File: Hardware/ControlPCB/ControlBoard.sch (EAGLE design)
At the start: 14 parts, among them IC1 TPS774

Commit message: Some PCB changes
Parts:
- added R7: 36k, resistor:R-EU_M2012
- added S2: DTSM-6, switch-tact:DTSM-6
- R4, R5: value (none) -> 0
- S1: device SparkFun-Electromechanical:SWITCH-MOMENTARY-2SMD-2 -> switch-tact:DTSM-6
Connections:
- net !RST: now also S2.1, S2.2
- net GND: now also R7.2, S1.2, S2.3, S2.4; no longer X2-4.1
- net GPIO0: now also S1.3, S1.4; no longer S1.2
- net OE: now also R7.1
- net VCC: now also X2-4.1
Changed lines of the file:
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@@
 <part name="R2" library="resistor" deviceset="R-EU_" device="R1206" value="4.7K"/>
 <part name="R3" library="resistor" deviceset="R-EU_" device="R1206" value="4.7K"/>
-<part name="S1" library="SparkFun-Electromechanical" deviceset="SWITCH-MOMENTARY-2" device="SMD-2" value="FlashSW"/>
+<part name="S1" library="switch-tact" deviceset="DTSM-6" device="" value="FlashSW"/>
 <part name="U1" library="esp8266modules" deviceset="ESP12E" device="SMD"/>
 <part name="IC1" library="texas" deviceset="TPS774*" device=""/>
@@
 <part name="X1" library="con-amp" deviceset="SMDTOP-20" device=""/>
 <part name="X2" library="con-amp" deviceset="SMDTOP-4" device=""/>
-<part name="R4" library="resistor" deviceset="R-EU_" device="R5025W"/>
-<part name="R5" library="resistor" deviceset="R-EU_" device="R5025W"/>
+<part name="R4" library="resistor" deviceset="R-EU_" device="R5025W" value="0"/>
+<part name="R5" library="resistor" deviceset="R-EU_" device="R5025W" value="0"/>
 <part name="R6" library="SparkFun-Passives" deviceset="SOLDERJUMPER" device="TRACE" value=""/>
 <part name="SJ1" library="SparkFun-Passives" deviceset="SOLDERJUMPER" device="TRACE" value=""/>
+<part name="R7" library="resistor" deviceset="R-EU_" device="M2012" value="36k"/>
+<part name="S2" library="switch-tact" deviceset="DTSM-6" device=""/>
 </parts>
 <sheets>
@@
 <instance part="R2" gate="G$1" x="88.9" y="119.38" rot="R180"/>
 <instance part="R3" gate="G$1" x="88.9" y="127" rot="R180"/>
-<instance part="S1" gate="G$1" x="88.9" y="142.24" rot="MR0"/>
+<instance part="S1" gate="G$1" x="88.9" y="142.24" rot="MR270"/>
 <instance part="U1" gate="G$1" x="101.6" y="104.14"/>
 <instance part="IC1" gate="G$1" x="160.02" y="137.16"/>
@@
 <instance part="R6" gate="1" x="154.94" y="99.06"/>
 <instance part="SJ1" gate="1" x="154.94" y="93.98"/>
+<instance part="R7" gate="G$1" x="154.94" y="116.84"/>
+<instance part="S2" gate="G$1" x="88.9" y="154.94" rot="R270"/>
 </instances>
 <busses>
@@
 <label x="96.52" y="142.24" size="1.778" layer="95"/>
 <pinref part="S1" gate="G$1" pin="1"/>
+<pinref part="S1" gate="G$1" pin="2"/>
+<wire x1="93.98" y1="139.7" x2="93.98" y2="142.24" width="0.1524" layer="91"/>
 </segment>
 <segment>
@@
 </segment>
 <segment>
-<pinref part="X2" gate="-4" pin="1"/>
-<wire x1="127" y1="134.62" x2="121.92" y2="134.62" width="0.1524" layer="91"/>
+<pinref part="R7" gate="G$1" pin="2"/>
+<wire x1="160.02" y1="116.84" x2="165.1" y2="116.84" width="0.1524" layer="91"/>
+<label x="165.1" y="116.84" size="1.778" layer="95"/>
+</segment>
+<segment>
+<pinref part="S2" gate="G$1" pin="3"/>
+<wire x1="93.98" y1="154.94" x2="96.52" y2="154.94" width="0.1524" layer="91"/>
+<pinref part="S2" gate="G$1" pin="4"/>
+<wire x1="93.98" y1="152.4" x2="93.98" y2="154.94" width="0.1524" layer="91"/>
+<label x="96.52" y="154.94" size="1.778" layer="95"/>
 </segment>
 </net>
@@
 <label x="63.5" y="119.38" size="1.778" layer="95"/>
 </segment>
+<segment>
+<pinref part="R7" gate="G$1" pin="1"/>
+<wire x1="149.86" y1="116.84" x2="144.78" y2="116.84" width="0.1524" layer="91"/>
+<label x="144.78" y="116.84" size="1.778" layer="95" rot="MR0"/>
+</segment>
 </net>
 <net name="MOSI" class="2">
@@
 <wire x1="83.82" y1="142.24" x2="81.28" y2="142.24" width="0.1524" layer="91"/>
 <label x="81.28" y="142.24" size="1.778" layer="95" rot="MR0"/>
-<pinref part="S1" gate="G$1" pin="2"/>
+<pinref part="S1" gate="G$1" pin="3"/>
+<pinref part="S1" gate="G$1" pin="4"/>
+<wire x1="83.82" y1="139.7" x2="83.82" y2="142.24" width="0.1524" layer="91"/>
 </segment>
 <segment>
@@
 <pinref part="C3" gate="G$1" pin="+"/>
 </segment>
+<segment>
+<pinref part="X2" gate="-4" pin="1"/>
+<wire x1="127" y1="134.62" x2="121.92" y2="134.62" width="0.1524" layer="91"/>
+<label x="121.92" y="134.62" size="1.778" layer="95" rot="MR0"/>
+</segment>
 </net>
 <net name="!RST" class="2">
@@
 <wire x1="78.74" y1="111.76" x2="83.82" y2="111.76" width="0.1524" layer="91"/>
 </segment>
-</net>
+<segment>
+<pinref part="S2" gate="G$1" pin="1"/>
+<wire x1="83.82" y1="154.94" x2="81.28" y2="154.94" width="0.1524" layer="91"/>
+<pinref part="S2" gate="G$1" pin="2"/>
+<wire x1="83.82" y1="152.4" x2="83.82" y2="154.94" width="0.1524" layer="91"/>
+<label x="81.28" y="154.94" size="1.778" layer="95" rot="MR0"/>
+</segment>
+</net>

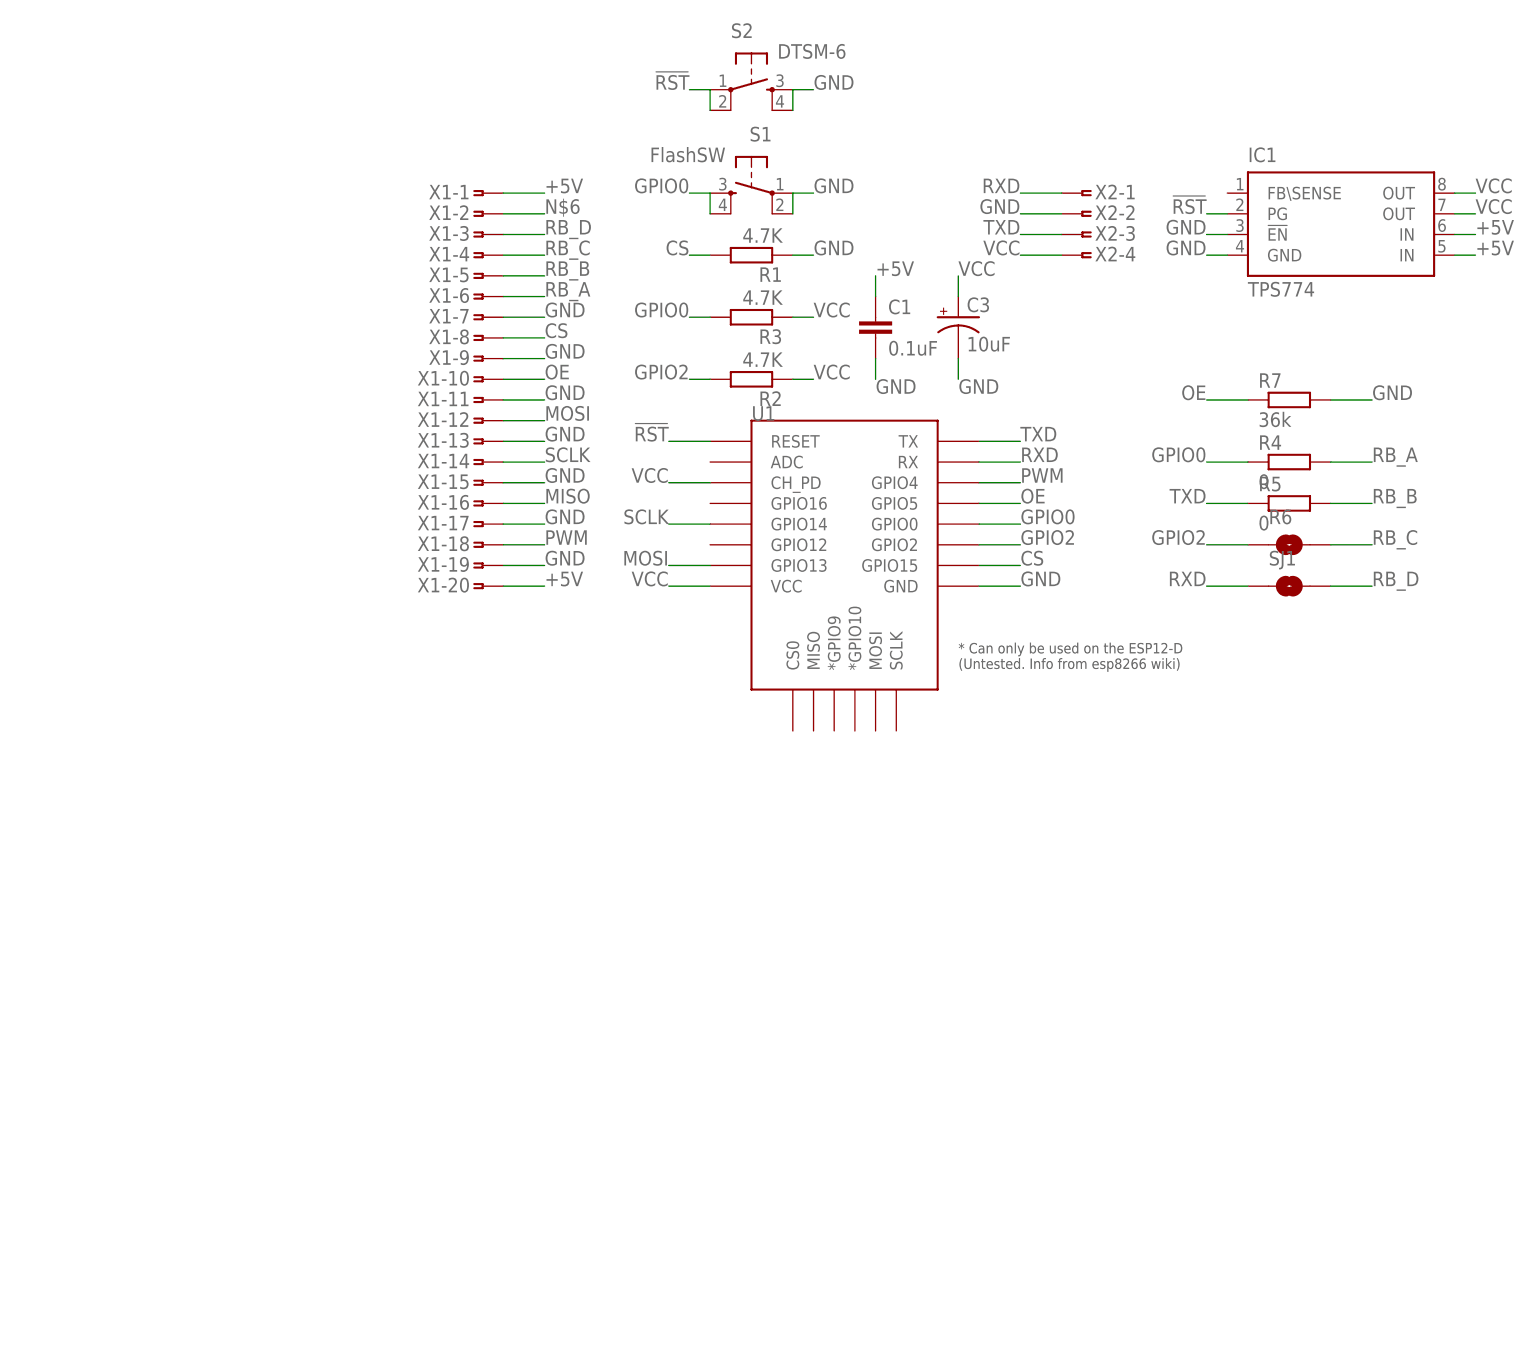
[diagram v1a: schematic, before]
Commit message: Updated schematics and pcb
Cleaned up schematics and new board layout with milling code files.
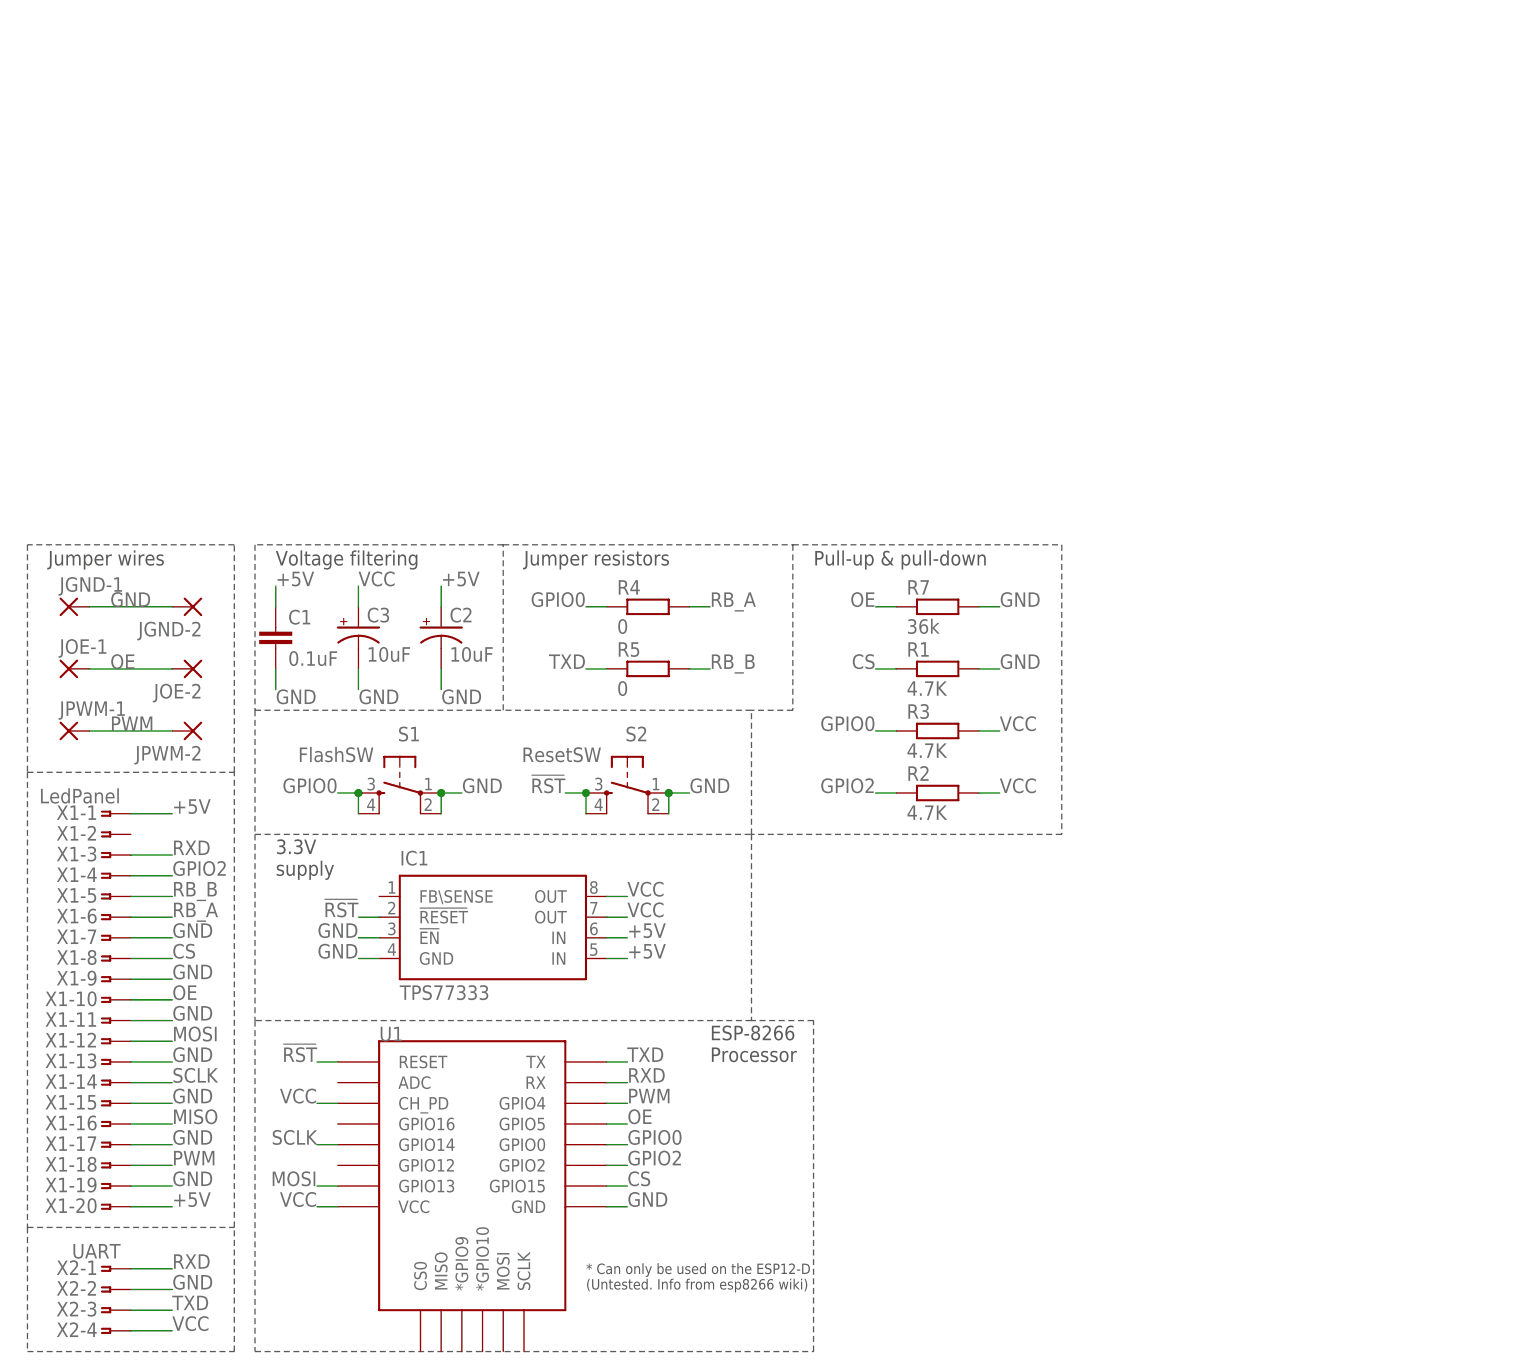
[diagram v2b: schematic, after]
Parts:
- removed R6, SJ1: SOLDERJUMPERTRACE, SparkFun-Passives:SOLDERJUMPERTRACE
- added C2: 10uF, SparkFun-Capacitors:10UF-20V-10%(TANT)
- added JGND-1, JGND-2, JOE-1, JOE-2, JPWM-1, JPWM-2: (no value), wirepad:SMD2
- IC1: value TPS774 -> TPS77333; device texas:TPS774 -> texas:TPS77333
- S2: value DTSM-6 -> ResetSW
- X1: value (none) -> LedPanel
- X2: value (none) -> UART
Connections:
- removed net N$6: X1-2.1
- removed net RB_C: R6.2, X1-4.1
- removed net RB_D: SJ1.2, X1-3.1
- net !RST: now also IC1.!RESET, S2.3, S2.4; no longer IC1.PG, S2.1, S2.2
- net +5V: now also C2.+
- net CS: now also R1.1; no longer R1.2
- net GND: now also C2.-, JGND-1.P, JGND-2.P, R1.2, S2.1, S2.2; no longer R1.1, S2.3, S2.4
- net GPIO0: now also R3.1; no longer R3.2
- net GPIO2: now also R2.1, X1-4.1; no longer R2.2, R6.1
- net OE: now also JOE-1.P, JOE-2.P
- net PWM: now also JPWM-1.P, JPWM-2.P
- net RXD: now also X1-3.1; no longer SJ1.1
- net VCC: now also R2.2, R3.2; no longer R2.1, R3.1
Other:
- note added: "3.3V supply"
- note added: "ESP-8266 Processor"
- note added: "Jumper resistors"
- note added: "Jumper wires"
- note added: "Pull-up & pull-down"
- note added: "Voltage filtering"
- moved on the sheet: C1, C3, IC1, R1, R2, R3, R4, R5, R7, S1, S2, U1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
